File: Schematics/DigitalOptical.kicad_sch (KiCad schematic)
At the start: 114 parts, among them Q1 BSS138, Q2 BSS138, Q3 BSS138, Q4 BSS138, U48 LM1117-3.3, U49 PCF8575, U50 PC817, U51 PC817, U52 PC817, U53 PC817, U54 PC817, U55 PC817, U56 PC817, U57 PC817, U58 PC817, U59 PC817, U60 PC817, U61 PC817, U62 PC817, U63 PC817, U64 PC817, U65 PC817, U66 PC817, U67 PC817, U68 PC817, U69 PC817, U70 PC817, U71 PC817, U72 PC817, U73 PC817, U74 PC817, U75 PC817, U76 PC817, U77 PC817, U78 PC817, U79 PC817, U80 PC817, U81 PC817, U82 PCF8575, U83 LM1117-3.3

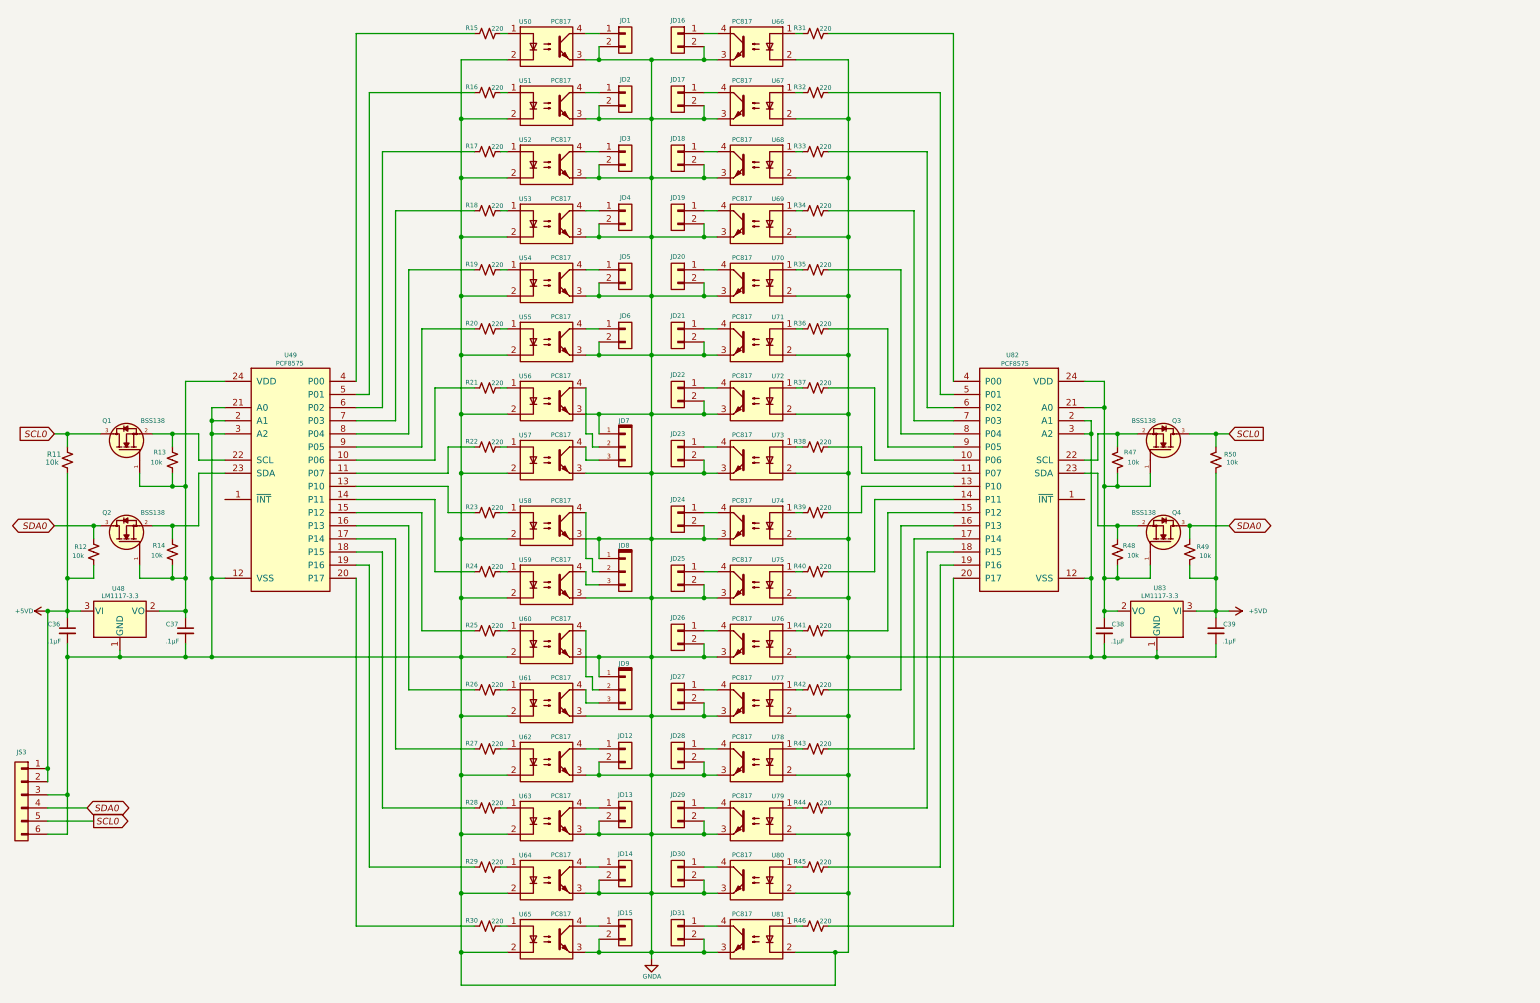
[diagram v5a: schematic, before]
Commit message: Update with noise filter & VCA as well as envelope generator software shell.
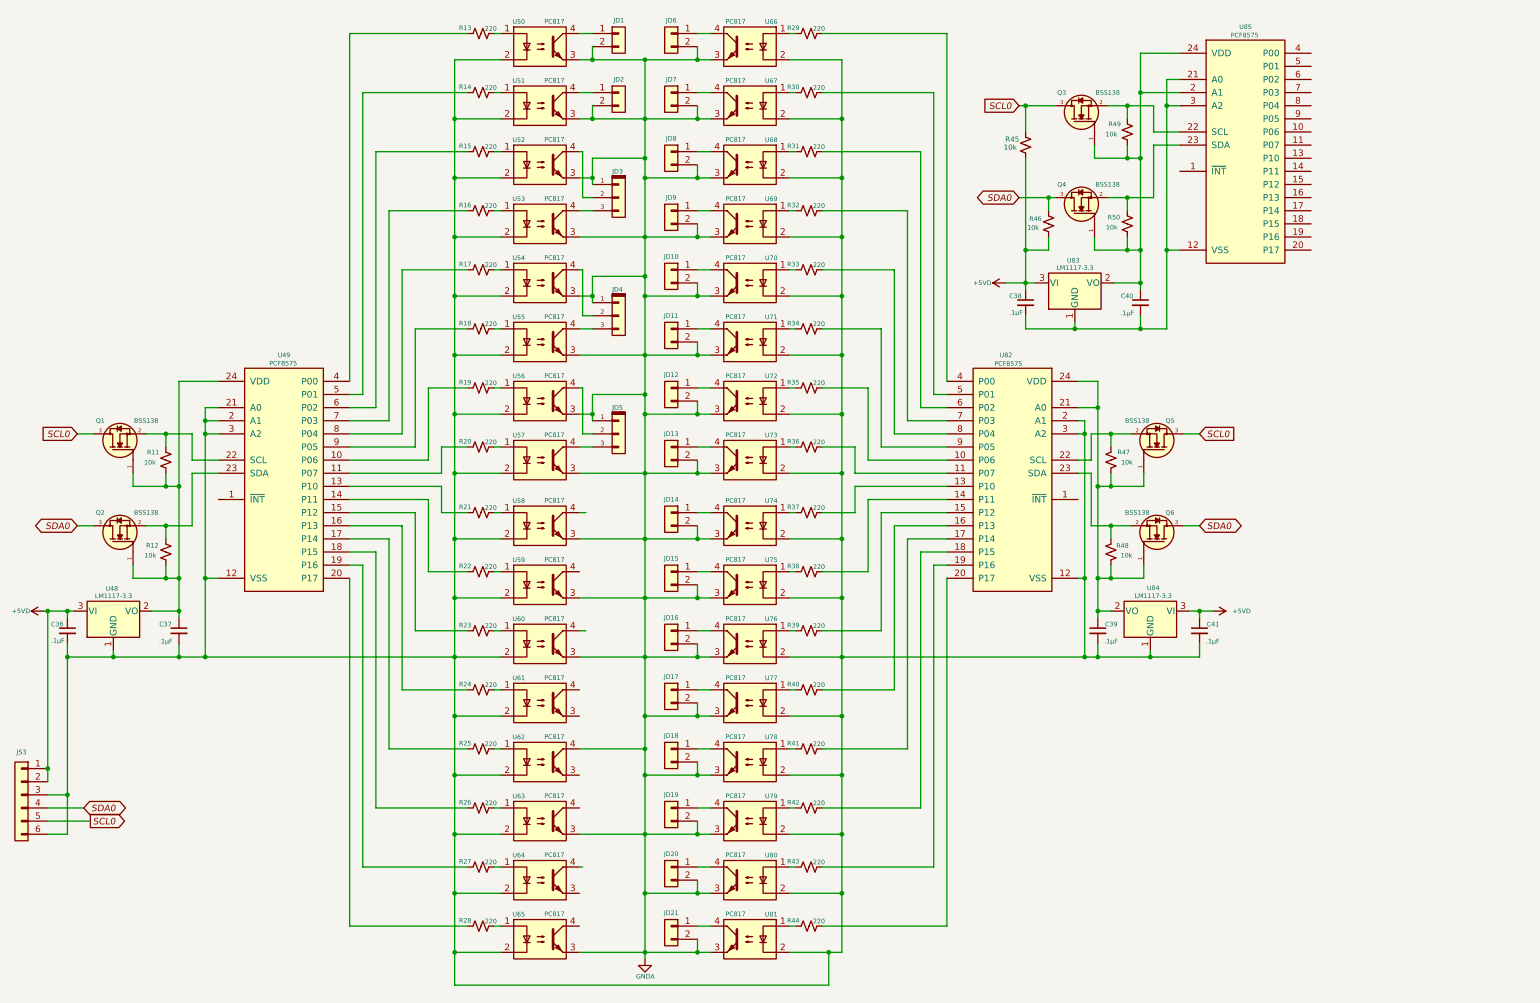
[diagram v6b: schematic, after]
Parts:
- removed JD12, JD13, JD14, JD15, JD3, JD4, JD5, JD6: From 12v Analog, symbol Connector_Generic:Conn_01x02
- removed R11, R12: 10k, symbol Device:R_Small_US
- added C38, C40: .1µF, symbol Device:C_Small
- added Q3, Q4: BSS138, digikey-footprints:SOT-23-3, symbol dk_Transistors-FETs-MOSFETs-Single:BSS138
- added R45, R46: 10k, symbol Device:R_Small_US
- added U83: LM1117-3.3, symbol Regulator_Linear:LM1117-3.3
- added U85: PCF8575, IPC7351-Nominal:SOP65P775X200-24, symbol NXP:PCF8575
- renumbered C38 to C39, C39 to C41, JD20 to JD10, JD21 to JD11, JD22 to JD12, JD23 to JD13, JD24 to JD14, JD25 to JD15, JD26 to JD16, JD27 to JD17, JD28 to JD18, JD29 to JD19, JD30 to JD20, JD31 to JD21, JD7 to JD3, JD8 to JD4, JD9 to JD5, JD16 to JD6, JD17 to JD7, JD18 to JD8, JD19 to JD9, Q3 to Q5, Q4 to Q6, R13 to R11, R14 to R12, R15 to R13, R16 to R14, R17 to R15, R18 to R16, R19 to R17, R20 to R18, R21 to R19, R22 to R20, R23 to R21, R24 to R22, R25 to R23, R26 to R24, R27 to R25, R28 to R26, R29 to R27, R30 to R28, R31 to R29, R32 to R30, R33 to R31, R34 to R32, R35 to R33, R36 to R34, R37 to R35, R38 to R36, R39 to R37, R40 to R38, R41 to R39, R42 to R40, R43 to R41, R44 to R42, R45 to R43, R46 to R44, U83 to U84
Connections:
- net +5VD: now also C38.1, R45.2, R46.2, U83.3 (VI); no longer R49.2, R50.2
- net GNDA: now also U62.4; no longer U61.3, U62.3, U64.3
- net SCL0: now also Q3.3, R45.1; no longer R50.1
- net SDA0: now also Q4.3, R46.1; no longer R49.1
- net at U54.4: now also JD4.2 (Pin_2)
- net at U56.4: now also JD5.2 (Pin_2); no longer JD3.2 (Pin_2)
- net at U53.4: now also JD3.3 (Pin_3)
- net at U55.4: now also JD4.3 (Pin_3)
- net at U58.4: no longer JD4.2 (Pin_2)
- net at U60.4: no longer JD5.2 (Pin_2)
- net at U52.4: now also JD3.2 (Pin_2)
- net at U57.4: now also JD5.3 (Pin_3); no longer JD3.3 (Pin_3)
- net at U59.4: no longer JD4.3 (Pin_3)
- net at U61.4: no longer JD5.3 (Pin_3)
- new net: C40.1, Q3.1, Q4.1, R49.2, R50.2, U83.2 (VO), U85.2 (A1), U85.24 (VDD)
- new net: Q4.2, R50.1, U85.23 (SDA)
- new net: C38.2, C40.2, U83.1 (GND), U85.12 (VSS), U85.21 (A0), U85.3 (A2)
- new net: Q3.2, R49.1, U85.22 (SCL)
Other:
- moved on the sheet: C37, C39, C41, JD10, JD11, JD12, JD13, JD14, JD15, JD16, JD17, JD18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

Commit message: Partial software with complete hardware on best 3 state filter with 4 outputs.
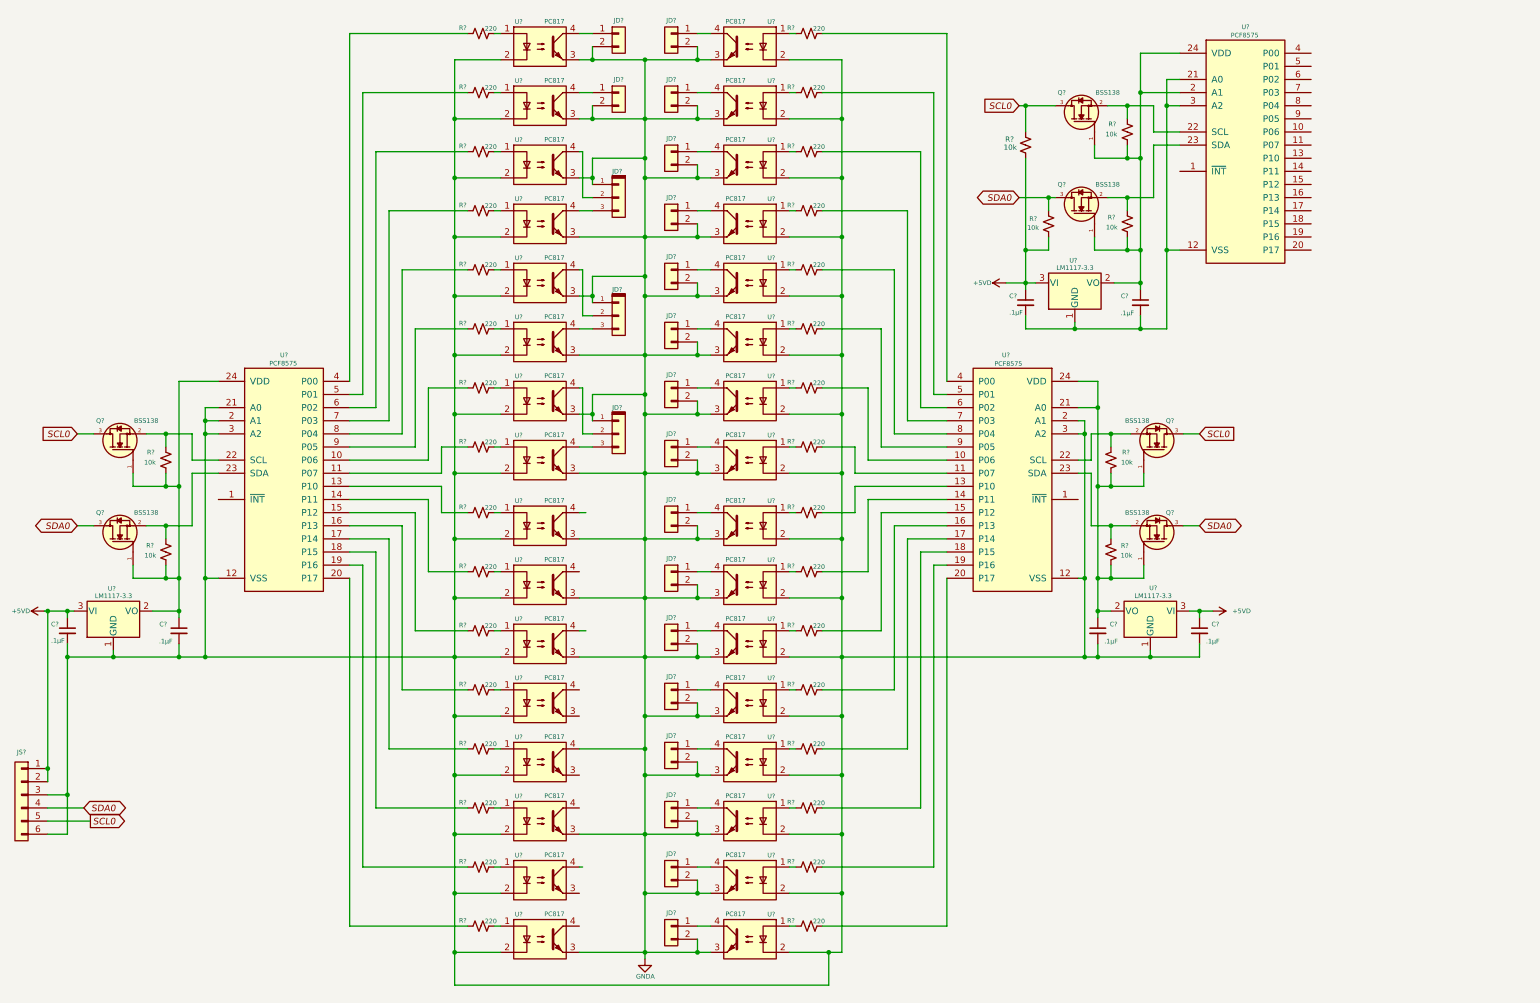
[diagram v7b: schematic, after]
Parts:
- renumbered C40 to C?, C37 to C?, C39 to C?, C41 to C?, C36 to C?, C38 to C?, JD9 to JD?, JD2 to JD?, JD12 to JD?, JD18 to JD?, JD6 to JD?, JD19 to JD?, JD3 to JD?, JD10 to JD?, JD8 to JD?, JD4 to JD?, JD11 to JD?, JD20 to JD?, JD7 to JD?, JD5 to JD?, JD17 to JD?, JD21 to JD?, JD14 to JD?, JD15 to JD?, JD13 to JD?, JD1 to JD?, JD16 to JD?, JS3 to JS?, Q1 to Q?, Q4 to Q?, Q6 to Q?, Q2 to Q?, Q5 to Q?, Q3 to Q?, R41 to R?, R45 to R?, R26 to R?, R18 to R?, R42 to R?, R35 to R?, R39 to R?, R36 to R?, R14 to R?, R34 to R?, R30 to R?, R22 to R?, R17 to R?, R23 to R?, R21 to R?, R13 to R?, R16 to R?, R44 to R?, R43 to R?, R31 to R?, R20 to R?, R37 to R?, R38 to R?, R15 to R?, R19 to R?, R28 to R?, R48 to R?, R11 to R?, R40 to R?, R47 to R?, R25 to R?, R49 to R?, R50 to R?, R29 to R?, R46 to R?, R24 to R?, R12 to R?, R32 to R?, R33 to R?, R27 to R?, U79 to U?, U66 to U?, U50 to U?, U69 to U?, U54 to U?, U56 to U?, U76 to U?, U55 to U?, U51 to U?, U75 to U?, U58 to U?, U60 to U?, U81 to U?, U78 to U?, U84 to U?, U83 to U?, U80 to U?, U49 to U?, U72 to U?, U71 to U?, U73 to U?, U52 to U?, U85 to U?, U62 to U?, U82 to U?, U65 to U?, U61 to U?, U48 to U?, U53 to U?, U67 to U?, U68 to U?, U63 to U?, U59 to U?, U74 to U?, U57 to U?, U64 to U?, U77 to U?, U70 to U?

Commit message: - Updated current libraries - New 7 inc display with ESP32S3 and second USB upload port - Start of I2C feeder interface slave on display.
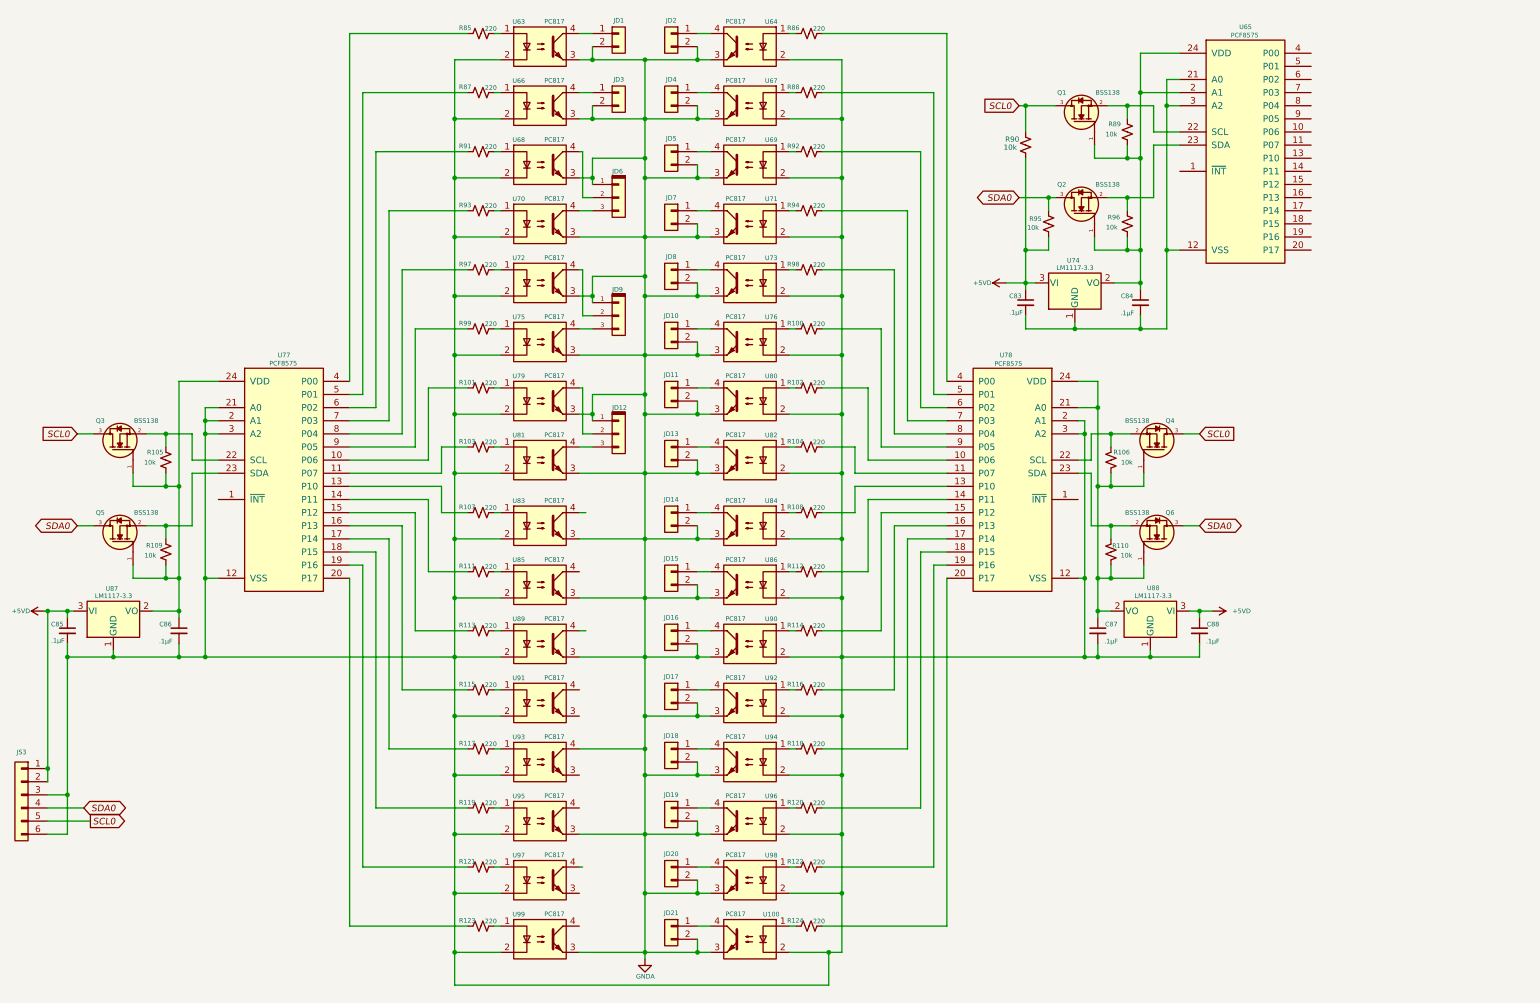
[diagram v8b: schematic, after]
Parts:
- gave numbers to parts that had none: 112
